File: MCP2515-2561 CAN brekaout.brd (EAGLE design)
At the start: 27.9 x 18.4 mm, 13 parts, among them IC1 MCP2515-I-ML, IC2 PRQV8.00CR1510Y00L, IC3 PESD5V2S2UT, IC4 MCP2561-2

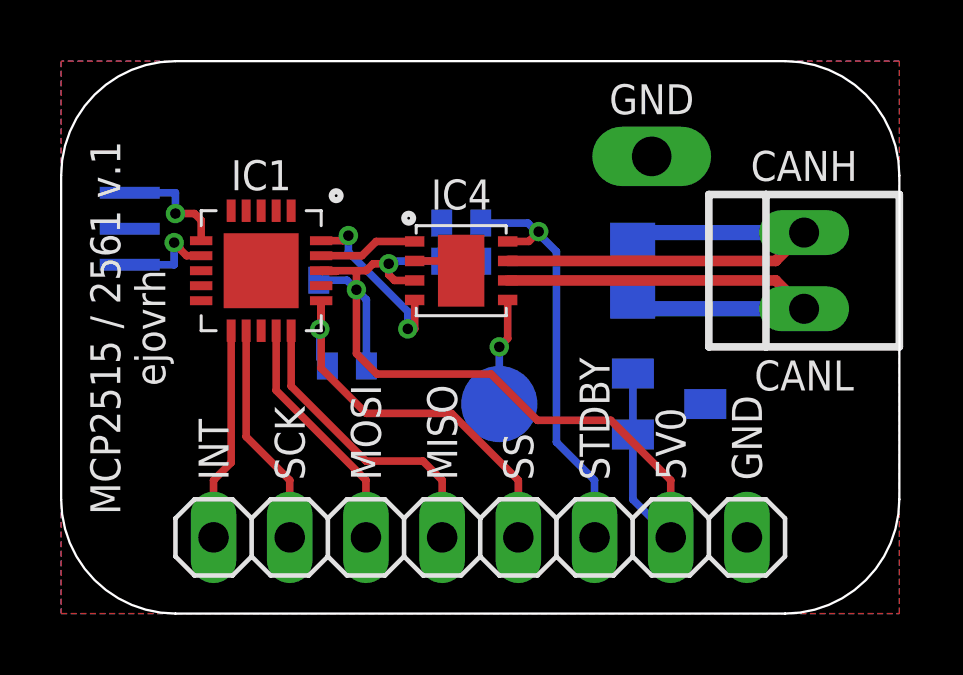
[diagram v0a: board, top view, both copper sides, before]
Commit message: - added pullup to reset pin on MCP2515-2561 CAN brekaout.brd
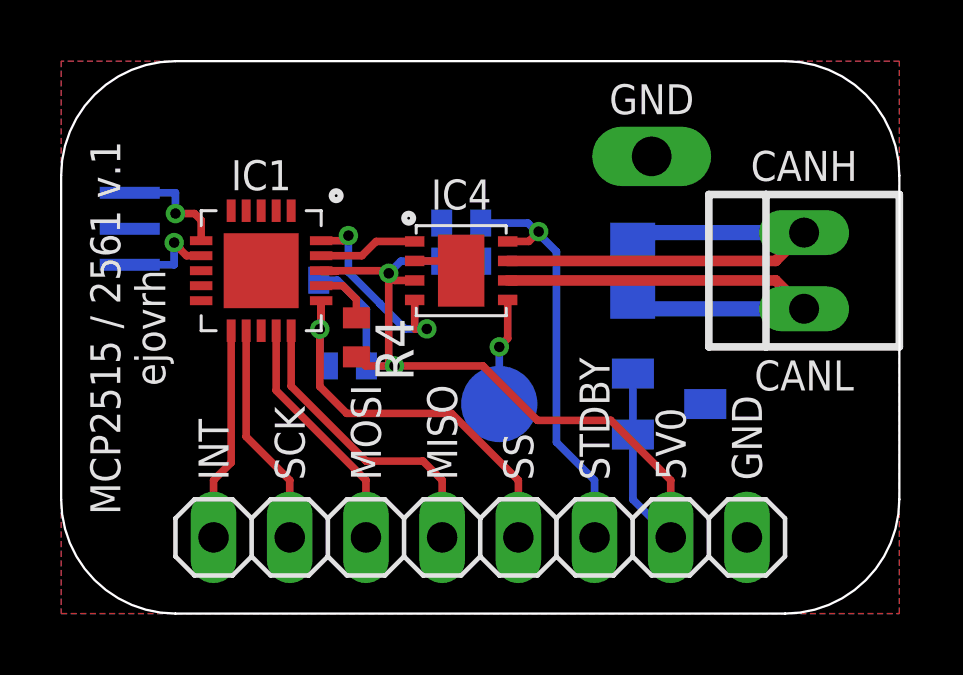
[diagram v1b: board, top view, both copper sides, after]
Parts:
- added R4: 10k, rcl:R0402
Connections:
- new net RESET: IC1.!RESET!, R4.1
- net 5V0: now also R4.2
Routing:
- net RESET: track 0.00 -> 2.01 mm
- net RXCAN: track 6.10 -> 6.97 mm
- net 5V0: track 34.2 -> 35.1 mm
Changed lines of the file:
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@@
 <?xml version="1.0" encoding="utf-8"?>
 <!DOCTYPE eagle SYSTEM "eagle.dtd">
-<eagle version="9.0.0">
+<eagle version="9.0.1">
 <drawing>
 <settings>
@@
 <attribute name="VALUE" x="24.13" y="5.715" size="1.27" layer="27" rot="R180"/>
 </element>
+<element name="R4" library="rcl" library_urn="urn:adsk.eagle:library:334" package="R0402" package3d_urn="urn:adsk.eagle:package:23547/1" value="10k" x="9.8425" y="9.2075" rot="R270"/>
 </elements>
 <signals>
@@
 <contactref element="IC4" pad="RXD"/>
 <via x="9.575" y="12.6" extent="1-16" drill="0.35"/>
-<via x="11.555" y="9.4905" extent="1-16" drill="0.35"/>
+<via x="12.19" y="9.4905" extent="1-16" drill="0.35"/>
 <wire x1="8.6675" y1="12.43" x2="9.405" y2="12.43" width="0.254" layer="1"/>
 <wire x1="9.405" y1="12.43" x2="9.575" y2="12.6" width="0.254" layer="1"/>
 <wire x1="11.785" y1="10.455" x2="11.785" y2="9.4905" width="0.254" layer="1"/>
-<wire x1="11.785" y1="9.4905" x2="11.555" y2="9.4905" width="0.254" layer="1"/>
-<wire x1="11.555" y1="9.4905" x2="11.555" y2="10.07093125" width="0.254" layer="16"/>
-<wire x1="9.575" y1="12.05093125" x2="9.575" y2="12.6" width="0.254" layer="16"/>
-<wire x1="11.555" y1="10.07093125" x2="9.575" y2="12.05093125" width="0.254" layer="16"/>
+<wire x1="11.785" y1="9.4905" x2="12.19" y2="9.4905" width="0.254" layer="1"/>
+<wire x1="12.19" y1="9.4905" x2="11.4645" y2="9.4905" width="0.254" layer="16"/>
+<wire x1="11.4645" y1="9.4905" x2="10.629" y2="10.326" width="0.254" layer="16"/>
+<wire x1="10.629" y1="10.326" x2="10.629" y2="10.33305625" width="0.254" layer="16"/>
+<wire x1="10.629" y1="10.33305625" x2="9.575" y2="11.38705625" width="0.254" layer="16"/>
+<wire x1="9.575" y1="11.38705625" x2="9.575" y2="12.6" width="0.254" layer="16"/>
 </signal>
 <signal name="CANH">
@@
 <contactref element="IC3" pad="CH1"/>
 <wire x1="11.1125" y1="11.105" x2="11.785" y2="11.105" width="0.254" layer="1"/>
-<via x="10.92" y="11.6605" extent="1-16" drill="0.35"/>
-<wire x1="10.16" y1="11.43" x2="9.8425" y2="11.43" width="0.254" layer="1"/>
-<wire x1="9.8425" y1="11.43" x2="8.6675" y2="11.43" width="0.254" layer="1"/>
-<via x="9.8425" y="10.795" extent="1-16" drill="0.35"/>
+<via x="10.92" y="11.343" extent="1-16" drill="0.35"/>
+<via x="11.1125" y="8.255" extent="1-16" drill="0.35"/>
 <wire x1="8.6675" y1="11.43" x2="8.6905" y2="11.407" width="0.254" layer="1"/>
 <wire x1="8.6905" y1="11.407" x2="9.17795" y2="11.407" width="0.254" layer="1"/>
-<wire x1="9.78995" y1="10.795" x2="9.8425" y2="10.795" width="0.254" layer="1"/>
-<wire x1="9.8425" y1="10.795" x2="9.8425" y2="11.43" width="0.254" layer="1"/>
-<wire x1="10.92" y1="11.6605" x2="10.39755625" y2="11.6605" width="0.254" layer="1"/>
-<wire x1="10.39755625" y1="11.6605" x2="10.21305625" y2="11.476" width="0.254" layer="1"/>
-<wire x1="10.21305625" y1="11.476" x2="10.206" y2="11.476" width="0.254" layer="1"/>
-<wire x1="10.206" y1="11.476" x2="10.16" y2="11.43" width="0.254" layer="1"/>
-<wire x1="10.92" y1="11.6605" x2="10.92" y2="11.2975" width="0.254" layer="1"/>
-<wire x1="10.92" y1="11.2975" x2="11.1125" y2="11.105" width="0.254" layer="1"/>
 <contactref element="JP1" pad="2"/>
 <wire x1="19.058" y1="8.001" x2="19.058" y2="5.969" width="0.254" layer="16"/>
@@
 <wire x1="20.32" y1="4.445" x2="20.32" y2="2.54" width="0.254" layer="1"/>
 <wire x1="18.323" y1="6.442" x2="15.875" y2="6.442" width="0.254" layer="1"/>
-<wire x1="9.8425" y1="10.795" x2="9.8425" y2="8.6645" width="0.254" layer="1"/>
-<wire x1="10.5235" y1="7.9835" x2="9.8425" y2="8.6645" width="0.254" layer="1"/>
-<wire x1="15.875" y1="6.442" x2="14.3335" y2="7.9835" width="0.254" layer="1"/>
-<wire x1="14.3335" y1="7.9835" x2="10.5235" y2="7.9835" width="0.254" layer="1"/>
-<wire x1="10.175" y1="8.255" x2="10.175" y2="10.4625" width="0.254" layer="16"/>
-<wire x1="10.175" y1="10.4625" x2="9.8425" y2="10.795" width="0.254" layer="16"/>
-<wire x1="8.5875" y1="11.1125" x2="9.525" y2="11.1125" width="0.254" layer="16"/>
-<wire x1="9.525" y1="11.1125" x2="9.8425" y2="10.795" width="0.254" layer="16"/>
-<wire x1="12.685" y1="11.7475" x2="11.007" y2="11.7475" width="0.254" layer="16"/>
-<wire x1="11.007" y1="11.7475" x2="10.92" y2="11.6605" width="0.254" layer="16"/>
+<wire x1="15.875" y1="6.442" x2="14.062" y2="8.255" width="0.254" layer="1"/>
 <wire x1="12.685" y1="13.0175" x2="12.685" y2="11.7475" width="0.254" layer="16"/>
+<contactref element="R4" pad="2"/>
+<wire x1="8.6675" y1="11.43" x2="10.7875" y2="11.43" width="0.254" layer="1"/>
+<wire x1="10.8745" y1="11.343" x2="11.1125" y2="11.105" width="0.254" layer="1"/>
+<wire x1="9.2075" y1="11.1125" x2="8.5875" y2="11.1125" width="0.254" layer="16"/>
+<wire x1="10.175" y1="8.255" x2="10.175" y2="10.145" width="0.254" layer="16"/>
+<wire x1="10.175" y1="10.145" x2="9.2075" y2="11.1125" width="0.254" layer="16"/>
+<wire x1="11.1125" y1="8.255" x2="10.175" y2="8.255" width="0.254" layer="16"/>
+<wire x1="11.1125" y1="8.255" x2="10.145" y2="8.255" width="0.254" layer="1"/>
+<wire x1="10.145" y1="8.255" x2="9.8425" y2="8.5575" width="0.254" layer="1"/>
+<wire x1="11.1125" y1="8.255" x2="14.062" y2="8.255" width="0.254" layer="1"/>
+<wire x1="10.92" y1="11.343" x2="11.3245" y2="11.7475" width="0.254" layer="16"/>
+<wire x1="11.3245" y1="11.7475" x2="12.685" y2="11.7475" width="0.254" layer="16"/>
+<wire x1="10.92" y1="11.343" x2="10.92" y2="8.4475" width="0.254" layer="1"/>
+<wire x1="10.92" y1="8.4475" x2="11.1125" y2="8.255" width="0.254" layer="1"/>
+<wire x1="10.92" y1="11.343" x2="10.8745" y2="11.343" width="0.254" layer="1"/>
+<wire x1="10.8745" y1="11.343" x2="10.7875" y2="11.43" width="0.254" layer="1"/>
 </signal>
 <signal name="OSC1">
@@
 <contactref element="JP1" pad="4"/>
 <wire x1="15.24" y1="2.54" x2="15.24" y2="4.445" width="0.254" layer="1"/>
-<wire x1="10.16705625" y1="6.67455625" x2="8.6675" y2="8.1741125" width="0.254" layer="1"/>
-<wire x1="8.6675" y1="8.1741125" x2="8.6675" y2="9.525" width="0.254" layer="1"/>
 <wire x1="8.6675" y1="9.525" x2="8.6675" y2="10.43" width="0.254" layer="1"/>
-<wire x1="13.01044375" y1="6.67455625" x2="10.16705625" y2="6.67455625" width="0.254" layer="1"/>
+<wire x1="13.01044375" y1="6.67455625" x2="9.51794375" y2="6.67455625" width="0.254" layer="1"/>
 <wire x1="15.24" y1="4.445" x2="13.01044375" y2="6.67455625" width="0.254" layer="1"/>
 <wire x1="8.6225" y1="9.4825" x2="8.6675" y2="9.5275" width="0.254" layer="1"/>
@@
 <wire x1="8.875" y1="8.255" x2="8.6225" y2="8.5075" width="0.254" layer="16"/>
 <wire x1="8.6225" y1="8.5075" x2="8.6225" y2="9.4825" width="0.254" layer="16"/>
+<wire x1="8.6225" y1="7.57" x2="8.6225" y2="9.4825" width="0.254" layer="1"/>
+<wire x1="9.51794375" y1="6.67455625" x2="8.6225" y2="7.57" width="0.254" layer="1"/>
 </signal>
 <signal name="SPI_SCK">
@@
 <wire x1="14.605" y1="8.89" x2="14.605" y2="6.985" width="0.254" layer="16"/>
 </signal>
+<signal name="RESET">
+<contactref element="IC1" pad="!RESET!"/>
+<contactref element="R4" pad="1"/>
+<wire x1="8.6675" y1="10.93" x2="8.6905" y2="10.907" width="0.254" layer="1"/>
+<wire x1="8.6675" y1="10.93" x2="9.39" y2="10.93" width="0.254" layer="1"/>
+<wire x1="9.39" y1="10.93" x2="9.8425" y2="10.4775" width="0.254" layer="1"/>
+<wire x1="9.8425" y1="10.4775" x2="9.8425" y2="9.8575" width="0.254" layer="1"/>
+</signal>
 </signals>
